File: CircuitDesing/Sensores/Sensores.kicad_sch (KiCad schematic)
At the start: 10 parts

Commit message: UnSoloUltrasonido
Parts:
- removed HC-SR04_1, HC-SR04_2, HC-SR04_3: Conn_01x04, symbol Connector_Generic:Conn_01x04
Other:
- note removed: "Sensor nivel de agua fertilizante 1"
- note removed: "Sensor nivel de agua fertilizante 2"
- note removed: "Sensor nivel de agua fertilizante 3"
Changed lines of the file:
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@@
-    (stroke (width 0) (type default) (color 0 0 0 0))
-  )
-  (wire (pts (xy 138.43 121.92) (xy 138.43 127))
-    (stroke (width 0) (type default) (color 0 0 0 0))
-  )
-  (wire (pts (xy 198.12 133.35) (xy 198.12 139.7))
-    (stroke (width 0) (type default) (color 0 0 0 0))
-  )
-  (wire (pts (xy 69.85 133.35) (xy 69.85 139.7))
     (stroke (width 0) (type default) (color 0 0 0 0))
   )
@@
     (stroke (width 0) (type default) (color 0 0 0 0))
   )
-  (wire (pts (xy 69.85 120.65) (xy 69.85 125.73))
-    (stroke (width 0) (type default) (color 0 0 0 0))
-  )
-  (wire (pts (xy 58.42 130.81) (xy 69.85 130.81))
-    (stroke (width 0) (type default) (color 0 0 0 0))
-  )
   (wire (pts (xy 50.8 97.79) (xy 69.85 97.79))
     (stroke (width 0) (type default) (color 0 0 0 0))
@@
     (stroke (width 0) (type default) (color 0 0 0 0))
   )
-  (wire (pts (xy 186.69 130.81) (xy 198.12 130.81))
-    (stroke (width 0) (type default) (color 0 0 0 0))
-  )
   (wire (pts (xy 138.43 100.33) (xy 138.43 105.41))
     (stroke (width 0) (type default) (color 0 0 0 0))
@@
     (stroke (width 0) (type default) (color 0 0 0 0))
   )
-  (wire (pts (xy 127 129.54) (xy 138.43 129.54))
-    (stroke (width 0) (type default) (color 0 0 0 0))
-  )
   (wire (pts (xy 69.85 90.17) (xy 69.85 95.25))
     (stroke (width 0) (type default) (color 0 0 0 0))
   )
-  (wire (pts (xy 186.69 128.27) (xy 198.12 128.27))
-    (stroke (width 0) (type default) (color 0 0 0 0))
-  )
   (wire (pts (xy 186.69 66.04) (xy 193.04 66.04))
     (stroke (width 0) (type default) (color 0 0 0 0))
   )
-  (wire (pts (xy 138.43 134.62) (xy 138.43 140.97))
-    (stroke (width 0) (type default) (color 0 0 0 0))
-  )
   (wire (pts (xy 69.85 100.33) (xy 69.85 105.41))
     (stroke (width 0) (type default) (color 0 0 0 0))
@@
     (stroke (width 0) (type default) (color 0 0 0 0))
   )
-  (wire (pts (xy 58.42 128.27) (xy 69.85 128.27))
-    (stroke (width 0) (type default) (color 0 0 0 0))
-  )
-  (wire (pts (xy 127 132.08) (xy 138.43 132.08))
-    (stroke (width 0) (type default) (color 0 0 0 0))
-  )
   (wire (pts (xy 193.04 66.04) (xy 193.04 67.31))
     (stroke (width 0) (type default) (color 0 0 0 0))
   )
-  (wire (pts (xy 198.12 120.65) (xy 198.12 125.73))
-    (stroke (width 0) (type default) (color 0 0 0 0))
-  )
   (text "Sensor de humedad de aire y temperatura 1" (at 40.64 91.44 0)
     (effects (font (size 1.27 1.27)) (justify left bottom))
   )
-  (text "Sensor nivel de agua fertilizante 1" (at 40.64 121.92 0)
-    (effects (font (size 1.27 1.27)) (justify left bottom))
-  )
   (text "Sensor de humedad de suelo 2" (at 109.22 91.44 0)
     (effects (font (size 1.27 1.27)) (justify left bottom))
   )
-  (text "Sensor nivel de agua fertilizante 3" (at 168.91 121.92 0)
-    (effects (font (size 1.27 1.27)) (justify left bottom))
-  )
   (text "Sensor de humedad de aire y temperatura 1" (at 40.64 58.42 0)
     (effects (font (size 1.27 1.27)) (justify left bottom))
@@
     (effects (font (size 1.27 1.27)) (justify left bottom))
   )
-  (text "Sensor nivel de agua fertilizante 2" (at 109.22 123.19 0)
-    (effects (font (size 1.27 1.27)) (justify left bottom))
-  )
   (text "Sensor de iluminación 1" (at 115.57 59.69 0)
     (effects (font (size 1.27 1.27)) (justify left bottom))
   )
-  (label "5v" (at 198.12 120.65 0)
-    (effects (font (size 1.27 1.27)) (justify left bottom))
-  )
   (label "5v" (at 198.12 87.63 0)
     (effects (font (size 1.27 1.27)) (justify left bottom))
@@
     (effects (font (size 1.27 1.27)) (justify left bottom))
   )
-  (label "5v" (at 69.85 120.65 0)
-    (effects (font (size 1.27 1.27)) (justify left bottom))
-  )
   (label "5v" (at 186.69 62.23 0)
     (effects (font (size 1.27 1.27)) (justify left bottom))
   )
-  (label "5v" (at 138.43 121.92 0)
-    (effects (font (size 1.27 1.27)) (justify left bottom))
-  )
   (hierarchical_label "DHT11_1_D" (shape input) (at 50.8 64.77 180)
     (effects (font (size 1.27 1.27)) (justify right))
@@
     (effects (font (size 1.27 1.27)) (justify right))
   )
-  (hierarchical_label "HC-SR04_0_Trig" (shape input) (at 186.69 128.27 180)
-    (effects (font (size 1.27 1.27)) (justify right))
-  )
   (hierarchical_label "HC-SR04_0_Echo" (shape input) (at 186.69 97.79 180)
     (effects (font (size 1.27 1.27)) (justify right))
@@
     (effects (font (size 1.27 1.27)) (justify right))
   )
-  (hierarchical_label "HC-SR04_0_Trig" (shape input) (at 127 129.54 180)
-    (effects (font (size 1.27 1.27)) (justify right))
-  )
   (hierarchical_label "HC-SR04_0_Trig" (shape input) (at 186.69 95.25 180)
     (effects (font (size 1.27 1.27)) (justify right))
   )
-  (hierarchical_label "HC-SR04_3_Echo" (shape input) (at 186.69 130.81 180)
-    (effects (font (size 1.27 1.27)) (justify right))
-  )
-  (hierarchical_label "HC-SR04_0_Trig" (shape input) (at 58.42 128.27 180)
-    (effects (font (size 1.27 1.27)) (justify right))
-  )
-  (hierarchical_label "HC-SR04_2_Echo" (shape input) (at 127 132.08 180)
-    (effects (font (size 1.27 1.27)) (justify right))
-  )
-  (hierarchical_label "HC-SR04_1_Echo" (shape input) (at 58.42 130.81 180)
-    (effects (font (size 1.27 1.27)) (justify right))
-  )
   (hierarchical_label "DHT11_2_D" (shape input) (at 50.8 97.79 180)
     (effects (font (size 1.27 1.27)) (justify right))
-  )
-  (symbol (lib_id "power:GND") (at 138.43 140.97 0) (unit 1)
-    (in_bom yes) (on_board yes) (fields_autoplaced)
-    (property "Reference" "#PWR?" (id 0) (at 138.43 147.32 0)
-      (effects (font (size 1.27 1.27)) hide)
-    )
-    (property "Value" "GND" (id 1) (at 138.43 146.05 0))
-    (property "Footprint" "" (id 2) (at 138.43 140.97 0)
-      (effects (font (size 1.27 1.27)) hide)
-    )
-    (property "Datasheet" "" (id 3) (at 138.43 140.97 0)
-      (effects (font (size 1.27 1.27)) hide)
-    )
-    (pin "1")
-  )
-  (symbol (lib_id "power:GND") (at 198.12 139.7 0) (unit 1)
-    (in_bom yes) (on_board yes) (fields_autoplaced)
-    (property "Reference" "#PWR?" (id 0) (at 198.12 146.05 0)
-      (effects (font (size 1.27 1.27)) hide)
-    )
-    (property "Value" "GND" (id 1) (at 198.12 144.78 0))
-    (property "Footprint" "" (id 2) (at 198.12 139.7 0)
-      (effects (font (size 1.27 1.27)) hide)
-    )
-    (property "Datasheet" "" (id 3) (at 198.12 139.7 0)
-      (effects (font (size 1.27 1.27)) hide)
-    )
-    (pin "1")
   )
   (symbol (lib_id "Connector_Generic:Conn_01x04") (at 203.2 95.25 0) (unit 1)
@@
     (pin "1")
   )
-  (symbol (lib_id "Connector_Generic:Conn_01x04") (at 74.93 128.27 0) (unit 1)
-    (in_bom yes) (on_board yes)
-    (property "Reference" "HC-SR04_1" (id 0) (at 77.47 128.2699 0)
-      (effects (font (size 1.27 1.27)) (justify left))
-    )
-    (property "Value" "Conn_01x04" (id 1) (at 77.47 130.8099 0)
-      (effects (font (size 1.27 1.27)) (justify left))
-    )
-    (property "Footprint" "" (id 2) (at 74.93 128.27 0)
-      (effects (font (size 1.27 1.27)) hide)
-    )
-    (property "Datasheet" "~" (id 3) (at 74.93 128.27 0)
-      (effects (font (size 1.27 1.27)) hide)
-    )
-    (pin "1")
-    (pin "2")
-    (pin "3")
-    (pin "4")
-  )
-  (symbol (lib_id "Connector_Generic:Conn_01x04") (at 203.2 128.27 0) (unit 1)
-    (in_bom yes) (on_board yes)
-    (property "Reference" "HC-SR04_3" (id 0) (at 205.74 128.2699 0)
-      (effects (font (size 1.27 1.27)) (justify left))
-    )
-    (property "Value" "Conn_01x04" (id 1) (at 205.74 130.8099 0)
-      (effects (font (size 1.27 1.27)) (justify left))
-    )
-    (property "Footprint" "" (id 2) (at 203.2 128.27 0)
-      (effects (font (size 1.27 1.27)) hide)
-    )
-    (property "Datasheet" "~" (id 3) (at 203.2 128.27 0)
-      (effects (font (size 1.27 1.27)) hide)
-    )
-    (pin "1")
-    (pin "2")
-    (pin "3")
-    (pin "4")
-  )
-  (symbol (lib_id "Connector_Generic:Conn_01x04") (at 143.51 129.54 0) (unit 1)
-    (in_bom yes) (on_board yes)
-    (property "Reference" "HC-SR04_2" (id 0) (at 146.05 129.5399 0)
-      (effects (font (size 1.27 1.27)) (justify left))
-    )
-    (property "Value" "Conn_01x04" (id 1) (at 146.05 132.0799 0)
-      (effects (font (size 1.27 1.27)) (justify left))
-    )
-    (property "Footprint" "" (id 2) (at 143.51 129.54 0)
-      (effects (font (size 1.27 1.27)) hide)
-    )
-    (property "Datasheet" "~" (id 3) (at 143.51 129.54 0)
-      (effects (font (size 1.27 1.27)) hide)
-    )
-    (pin "1")
-    (pin "2")
-    (pin "3")
-    (pin "4")
-  )
   (symbol (lib_id "power:GND") (at 69.85 72.39 0) (unit 1)
     (in_bom yes) (on_board yes) (fields_autoplaced)
@@
     (pin "4")
   )
-  (symbol (lib_id "power:GND") (at 69.85 139.7 0) (unit 1)
-    (in_bom yes) (on_board yes) (fields_autoplaced)
-    (property "Reference" "#PWR?" (id 0) (at 69.85 146.05 0)
-      (effects (font (size 1.27 1.27)) hide)
-    )
-    (property "Value" "GND" (id 1) (at 69.85 144.78 0))
-    (property "Footprint" "" (id 2) (at 69.85 139.7 0)
-      (effects (font (size 1.27 1.27)) hide)
-    )
-    (property "Datasheet" "" (id 3) (at 69.85 139.7 0)
-      (effects (font (size 1.27 1.27)) hide)
-    )
-    (pin "1")
-  )
 )

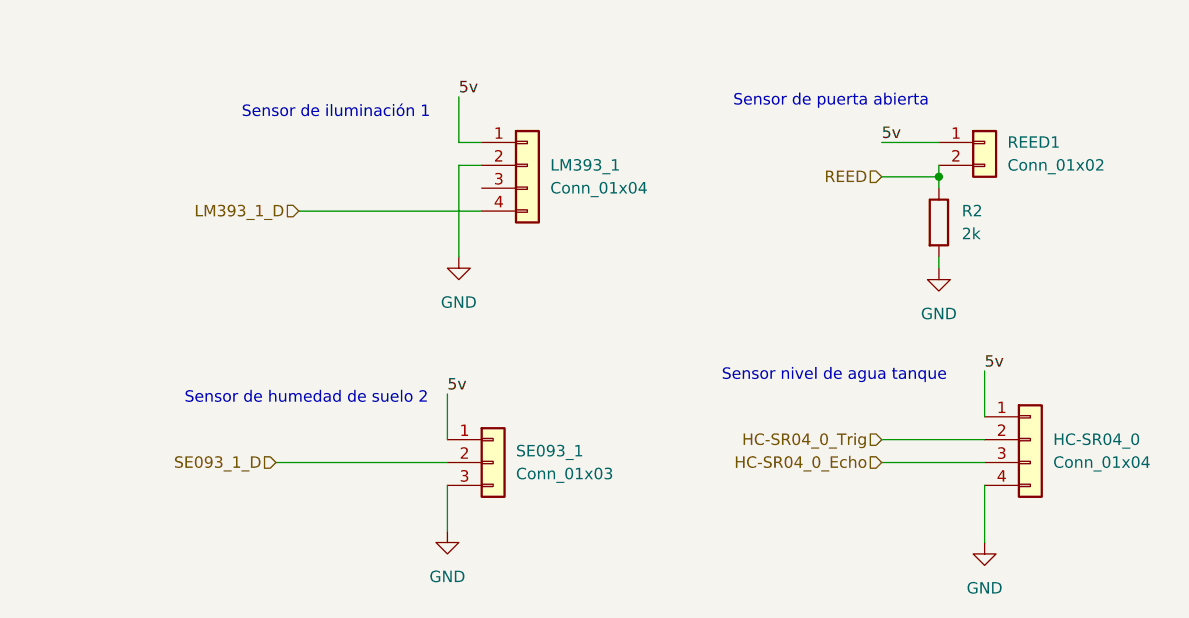
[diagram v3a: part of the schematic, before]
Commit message: Modificaciones generales
Modificaciones a esquemático,  interacción con otros grupos, sistema de potencia.
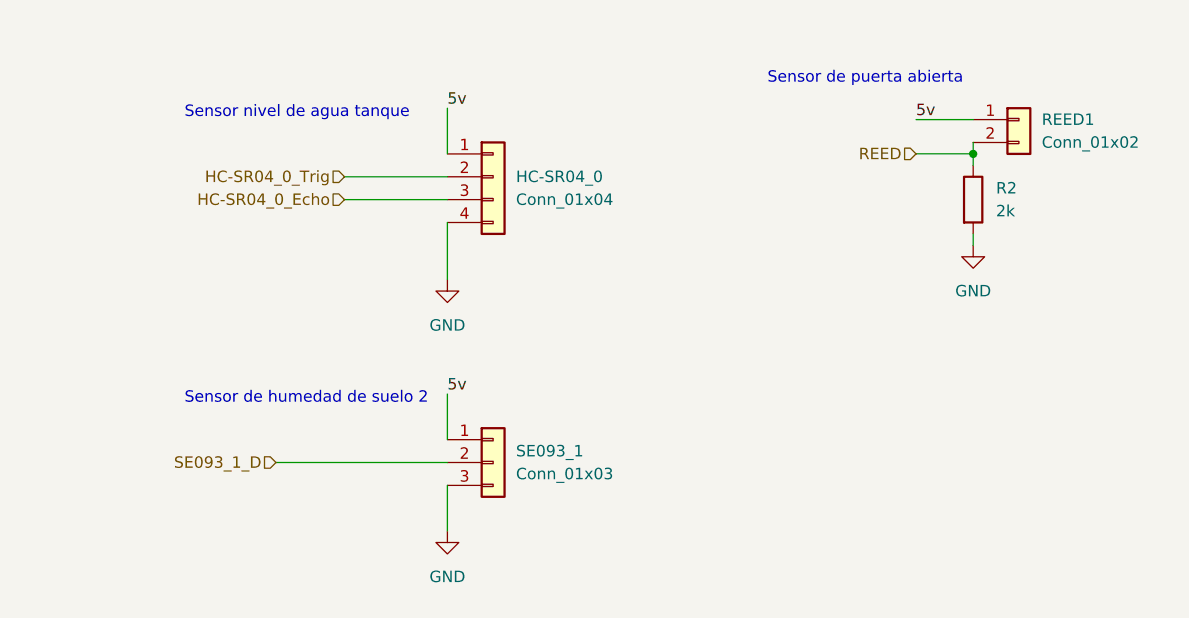
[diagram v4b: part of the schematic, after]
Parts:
- removed LM393_1: Conn_01x04, symbol Connector_Generic:Conn_01x04
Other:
- note removed: "Sensor de iluminación 1"
- moved on the sheet: HC-SR04_0, R2, REED1

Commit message: Huellas
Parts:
- DHT11_1, DHT11_2, SE093_1: footprint (none) -> Connector_JST:JST_EH_B3B-EH-A_1x03_P2.50mm_Vertical
- HC-SR04_0: footprint (none) -> Connector_JST:JST_EH_B4B-EH-A_1x04_P2.50mm_Vertical
- REED1: footprint (none) -> Connector_JST:JST_EH_B2B-EH-A_1x02_P2.50mm_Vertical
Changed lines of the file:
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@@
       (effects (font (size 1.27 1.27)) (justify left))
     )
-    (property "Footprint" "" (id 2) (at 143.51 66.04 0)
+    (property "Footprint" "Connector_JST:JST_EH_B4B-EH-A_1x04_P2.50mm_Vertical" (id 2) (at 143.51 66.04 0)
       (effects (font (size 1.27 1.27)) hide)
     )
@@
       (effects (font (size 1.27 1.27)) (justify left))
     )
-    (property "Footprint" "" (id 2) (at 143.51 97.79 0)
+    (property "Footprint" "Connector_JST:JST_EH_B3B-EH-A_1x03_P2.50mm_Vertical" (id 2) (at 143.51 97.79 0)
       (effects (font (size 1.27 1.27)) hide)
     )
@@
       (effects (font (size 1.27 1.27)) (justify left))
     )
-    (property "Footprint" "" (id 2) (at 74.93 64.77 0)
+    (property "Footprint" "Connector_JST:JST_EH_B3B-EH-A_1x03_P2.50mm_Vertical" (id 2) (at 74.93 64.77 0)
       (effects (font (size 1.27 1.27)) hide)
     )
@@
   (symbol (lib_id "power:GND") (at 69.85 105.41 0) (unit 1)
     (in_bom yes) (on_board yes) (fields_autoplaced)
-    (property "Reference" "#PWR?" (id 0) (at 69.85 111.76 0)
+    (property "Reference" "#PWR0107" (id 0) (at 69.85 111.76 0)
       (effects (font (size 1.27 1.27)) hide)
     )
@@
   (symbol (lib_id "power:GND") (at 138.43 105.41 0) (unit 1)
     (in_bom yes) (on_board yes) (fields_autoplaced)
-    (property "Reference" "#PWR?" (id 0) (at 138.43 111.76 0)
+    (property "Reference" "#PWR0106" (id 0) (at 138.43 111.76 0)
       (effects (font (size 1.27 1.27)) hide)
     )
@@
       (effects (font (size 1.27 1.27)) (justify left))
     )
-    (property "Footprint" "" (id 2) (at 74.93 97.79 0)
+    (property "Footprint" "Connector_JST:JST_EH_B3B-EH-A_1x03_P2.50mm_Vertical" (id 2) (at 74.93 97.79 0)
       (effects (font (size 1.27 1.27)) hide)
     )
@@
   (symbol (lib_id "power:GND") (at 196.85 73.66 0) (unit 1)
     (in_bom yes) (on_board yes) (fields_autoplaced)
-    (property "Reference" "#PWR?" (id 0) (at 196.85 80.01 0)
+    (property "Reference" "#PWR0109" (id 0) (at 196.85 80.01 0)
       (effects (font (size 1.27 1.27)) hide)
     )
@@
   (symbol (lib_id "power:GND") (at 138.43 77.47 0) (unit 1)
     (in_bom yes) (on_board yes) (fields_autoplaced)
-    (property "Reference" "#PWR?" (id 0) (at 138.43 83.82 0)
+    (property "Reference" "#PWR0104" (id 0) (at 138.43 83.82 0)
       (effects (font (size 1.27 1.27)) hide)
     )
@@
   (symbol (lib_id "power:GND") (at 69.85 72.39 0) (unit 1)
     (in_bom yes) (on_board yes) (fields_autoplaced)
-    (property "Reference" "#PWR?" (id 0) (at 69.85 78.74 0)
+    (property "Reference" "#PWR0108" (id 0) (at 69.85 78.74 0)
       (effects (font (size 1.27 1.27)) hide)
     )
@@
       (effects (font (size 1.27 1.27)) (justify left))
     )
-    (property "Footprint" "" (id 2) (at 201.93 59.69 0)
+    (property "Footprint" "Connector_JST:JST_EH_B2B-EH-A_1x02_P2.50mm_Vertical" (id 2) (at 201.93 59.69 0)
       (effects (font (size 1.27 1.27)) hide)
     )
